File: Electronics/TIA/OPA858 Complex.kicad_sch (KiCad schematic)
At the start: 16 parts, among them U4 ${SIM.PARAMS}

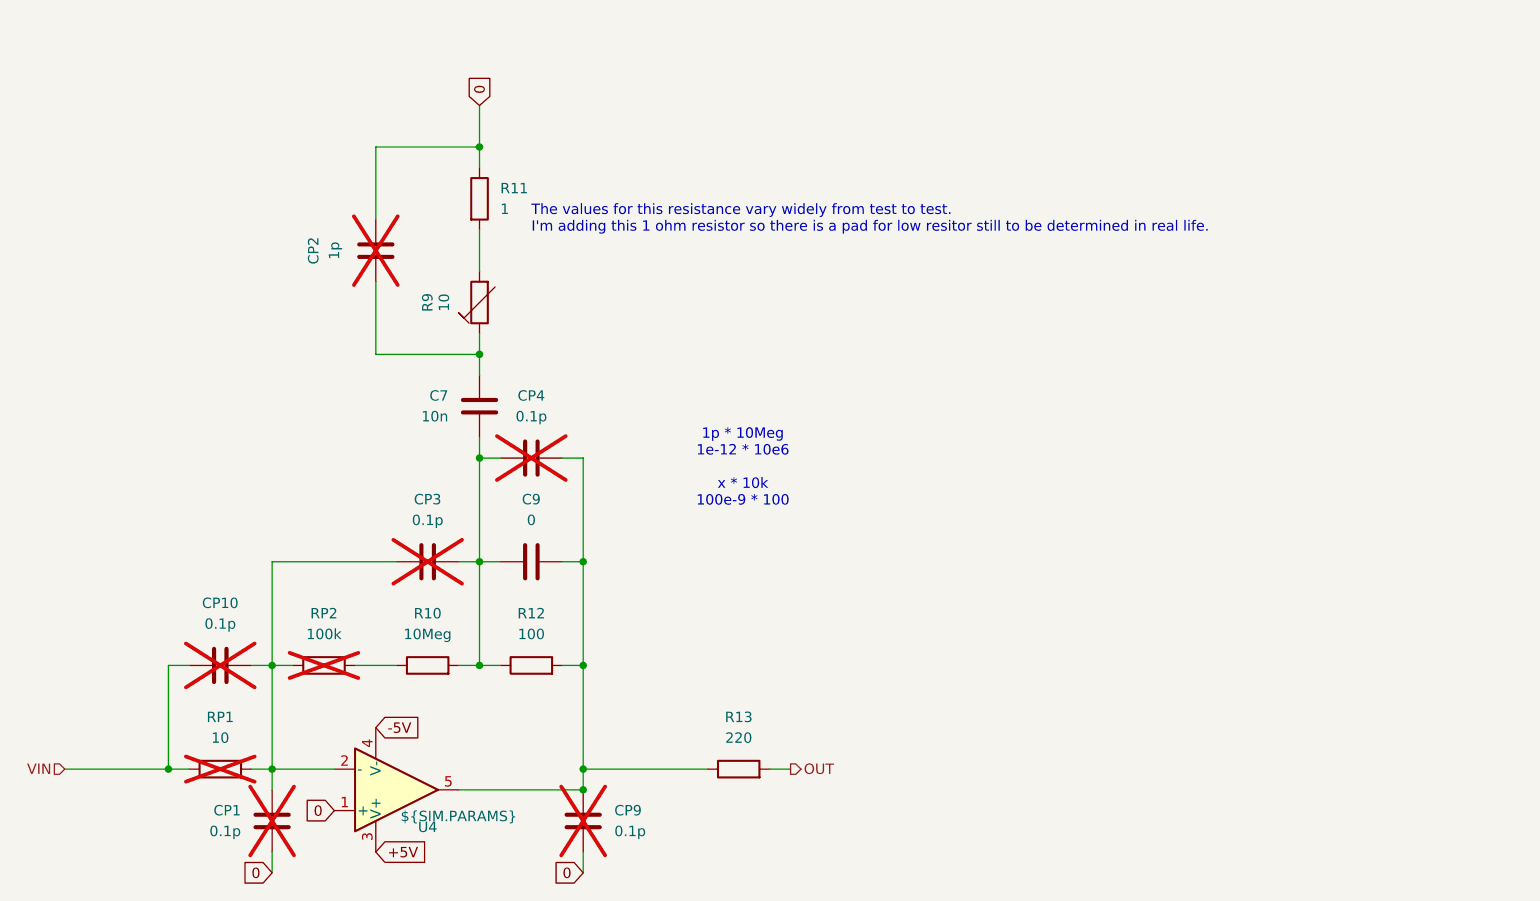
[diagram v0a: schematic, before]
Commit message: Create simpler stability simulation
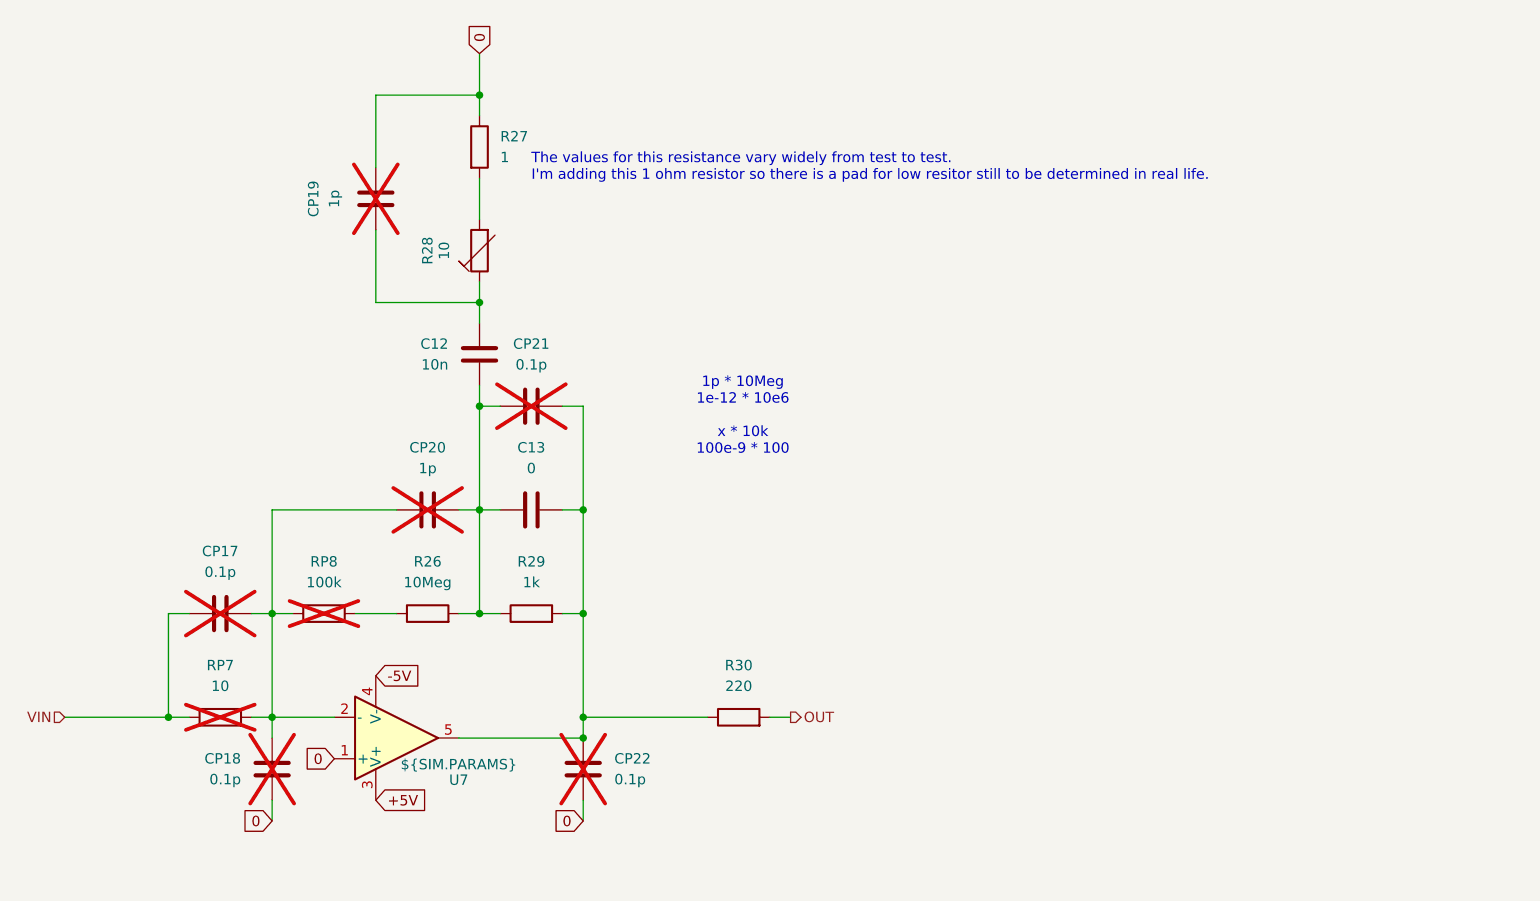
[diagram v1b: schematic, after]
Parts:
- removed C7: 10n, symbol Device:C
- removed C9: 0, symbol Device:C
- removed CP1, CP10, CP3, CP4, CP9: 0.1p, symbol Device:C
- removed CP2: 1p, symbol Device:C
- removed R10: 10Meg, symbol Device:R
- removed R11: 1, symbol Device:R
- removed R12: 100, symbol Device:R
- removed R13: 220, symbol Device:R
- removed R9: 10, symbol Device:R_Trim
- removed RP1: 10, symbol Device:R
- removed RP2: 100k, symbol Device:R
- removed U4: ${SIM.PARAMS}, symbol Simulation_SPICE:OPAMP
- added C12: 10n, symbol Device:C
- added C13: 0, symbol Device:C
- added CP17, CP18, CP21, CP22: 0.1p, symbol Device:C
- added CP19, CP20: 1p, symbol Device:C
- added R26: 10Meg, symbol Device:R
- added R27: 1, symbol Device:R
- added R28: 10, symbol Device:R_Trim
- added R29: 1k, symbol Device:R
- added R30: 220, symbol Device:R
- added RP7: 10, symbol Device:R
- added RP8: 100k, symbol Device:R
- added U7: ${SIM.PARAMS}, symbol Simulation_SPICE:OPAMP
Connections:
- net +5V: now also U7.3 (V+)
- net -5V: now also U7.4 (V-)
- net 0: now also CP18.2, CP19.2, CP22.1, R27.1, U7.1 (+)
- net OUT: now also R30.2
- net VIN: now also CP17.1, RP7.1
- new net: C12.2, C13.1, CP20.1, CP21.1, R26.2, R29.1
- new net: CP17.2, CP18.1, CP20.2, RP7.2, RP8.1, U7.2 (-)
- new net: R27.2, R28.2
- new net: C13.2, CP21.2, CP22.2, R29.2, R30.1, U7.5
- new net: C12.1, CP19.1, R28.1
- new net: R26.1, RP8.2
